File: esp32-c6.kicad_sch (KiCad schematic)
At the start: 38 parts, among them J1 USB_C_Receptacle_USB2.0_14P, J2 USB_C_Receptacle_USB2.0_14P, Q1 BC847BDW1, SW1 SW_Push, SW2 SW_Push, U1 CP2102N-Axx-xQFN28

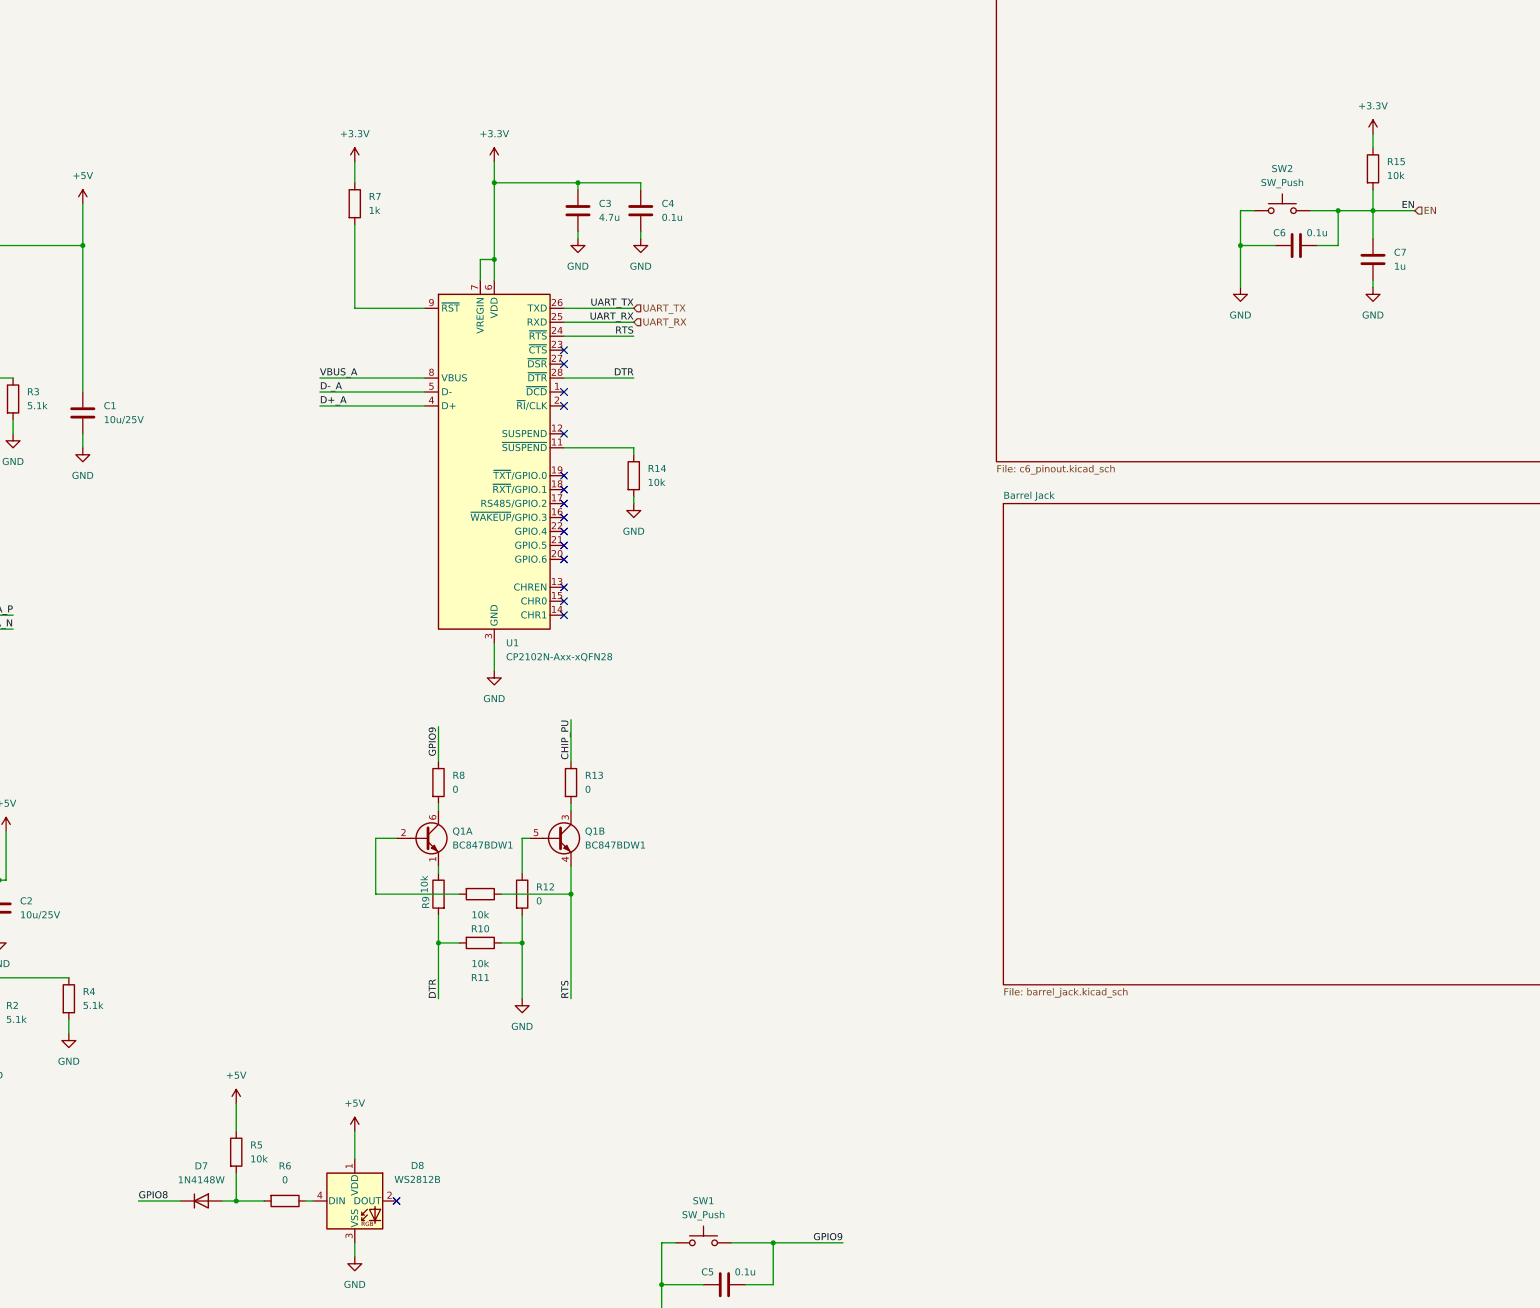
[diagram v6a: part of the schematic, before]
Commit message: layout + power pin traces
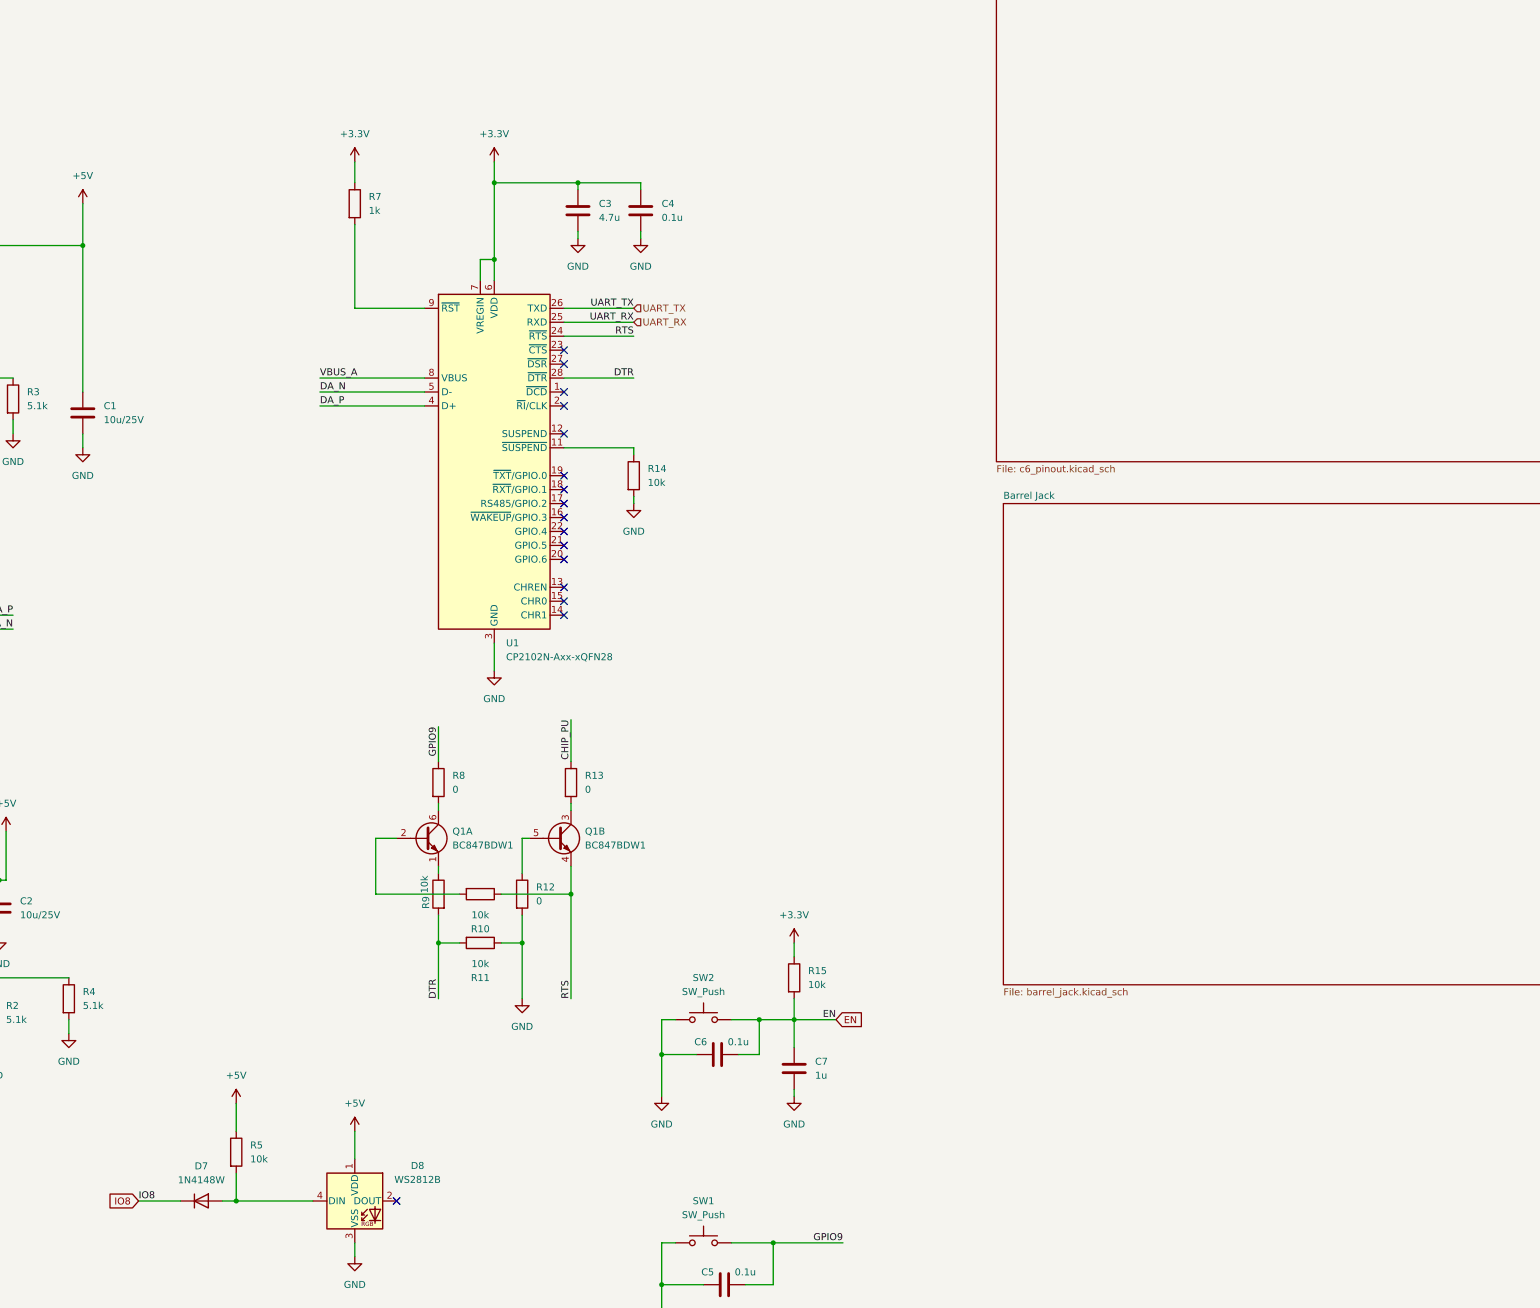
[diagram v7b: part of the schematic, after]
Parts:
- removed R6: 0, Resistor_SMD:R_0201_0603Metric, symbol Device:R
- R10, R14, R7, R9: footprint Resistor_SMD:R_0402_1005Metric -> Resistor_SMD:R_0201_0603Metric
- R11: footprint Resistor_SMD:R_0201_0603Metric_Pad0.64x0.40mm_HandSolder -> Resistor_SMD:R_0201_0603Metric
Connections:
- net D+_A is gone; now on net DA_P: U1.4 (D+)
- net D-_A is gone; now on net DA_N: U1.5 (D-)
- net at D7.2 (A), R5.2: now also D8.4 (DIN)
- net GPIO8 renamed IO8
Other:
- moved on the sheet: C6, C7, R15, SW2

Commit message: final tracing + pcb layers + colors
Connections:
- net IO12_DB_N renamed DB_N
- net IO13_DB_P renamed DB_P
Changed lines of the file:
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@@
 		)
 	)
-	(label "IO13_DB_P"
+	(label "DB_P"
 		(at 77.47 219.71 180)
 		(effects
@@
 	)
 	(label "DA_P"
-		(at 158.75 100.33 0)
+		(at 165.1 100.33 0)
 		(effects
 			(font
@@
 		)
 	)
-	(label "IO12_DB_N"
+	(label "IO12_N"
 		(at 87.63 214.63 180)
 		(effects
@@
 	)
 	(label "DA_N"
-		(at 158.75 97.79 0)
+		(at 165.1 97.79 0)
 		(effects
 			(font
@@
 		)
 	)
+	(global_label "DB_N"
+		(shape input)
+		(at 87.63 214.63 90)
+		(fields_autoplaced yes)
+		(effects
+			(font
+				(size 1.27 1.27)
+			)
+			(justify left)
+		)
+		(property "Intersheetrefs" "${INTERSHEET_REFS}"
+			(at 87.63 206.8067 90)
+			(effects
+				(font
+					(size 1.27 1.27)
+				)
+				(justify left)
+				(hide yes)
+			)
+		)
+	)
 	(global_label "IO8"
 		(shape input)
@@
 		)
 	)
+	(global_label "DB_P"
+		(shape input)
+		(at 77.47 219.71 90)
+		(fields_autoplaced yes)
+		(effects
+			(font
+				(size 1.27 1.27)
+			)
+			(justify left)
+		)
+		(property "Intersheetrefs" "${INTERSHEET_REFS}"
+			(at 77.47 211.9472 90)
+			(effects
+				(font
+					(size 1.27 1.27)
+				)
+				(justify left)
+				(hide yes)
+			)
+		)
+	)
 	(hierarchical_label "UART_TX"
 		(shape input)
@@
 		)
 	)
+	(netclass_flag ""
+		(length 2.54)
+		(shape round)
+		(at 158.75 100.33 0)
+		(fields_autoplaced yes)
+		(effects
+			(font
+				(size 1.27 1.27)
+			)
+			(justify left bottom)
+		)
+		(property "Netclass" "usb"
+			(at 159.4485 97.79 0)
+			(effects
+				(font
+					(size 1.27 1.27)
+				)
+				(justify left)
+			)
+		)
+		(property "Component Class" ""
+			(at -35.56 2.54 0)
+			(effects
+				(font
+					(size 1.27 1.27)
+					(italic yes)
+				)
+			)
+		)
+	)
+	(netclass_flag ""
+		(length 2.54)
+		(shape round)
+		(at 158.75 97.79 0)
+		(fields_autoplaced yes)
+		(effects
+			(font
+				(size 1.27 1.27)
+			)
+			(justify left bottom)
+		)
+		(property "Netclass" "usb"
+			(at 159.4485 95.25 0)
+			(effects
+				(font
+					(size 1.27 1.27)
+				)
+				(justify left)
+			)
+		)
+		(property "Component Class" ""
+			(at -35.56 0 0)
+			(effects
+				(font
+					(size 1.27 1.27)
+					(italic yes)
+				)
+			)
+		)
+	)
+	(netclass_flag ""
+		(length 2.54)
+		(shape round)
+		(at 102.87 140.97 0)
+		(fields_autoplaced yes)
+		(effects
+			(font
+				(size 1.27 1.27)
+			)
+			(justify left bottom)
+		)
+		(property "Netclass" "usb"
+			(at 103.5685 138.43 0)
+			(effects
+				(font
+					(size 1.27 1.27)
+				)
+				(justify left)
+			)
+		)
+		(property "Component Class" ""
+			(at -5.08 34.29 0)
+			(effects
+				(font
+					(size 1.27 1.27)
+					(italic yes)
+				)
+			)
+		)
+	)
+	(netclass_flag ""
+		(length 2.54)
+		(shape round)
+		(at 102.87 138.43 0)
+		(fields_autoplaced yes)
+		(effects
+			(font
+				(size 1.27 1.27)
+			)
+			(justify left bottom)
+		)
+		(property "Netclass" "usb"
+			(at 103.5685 135.89 0)
+			(effects
+				(font
+					(size 1.27 1.27)
+				)
+				(justify left)
+			)
+		)
+		(property "Component Class" ""
+			(at -5.08 31.75 0)
+			(effects
+				(font
+					(size 1.27 1.27)
+					(italic yes)
+				)
+			)
+		)
+	)
